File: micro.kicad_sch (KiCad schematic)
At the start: 25 parts, among them SW1 BOOT, SW2 RST, U1 RP2040, U5 W25Q128JVSIQ, Y1 12MHz

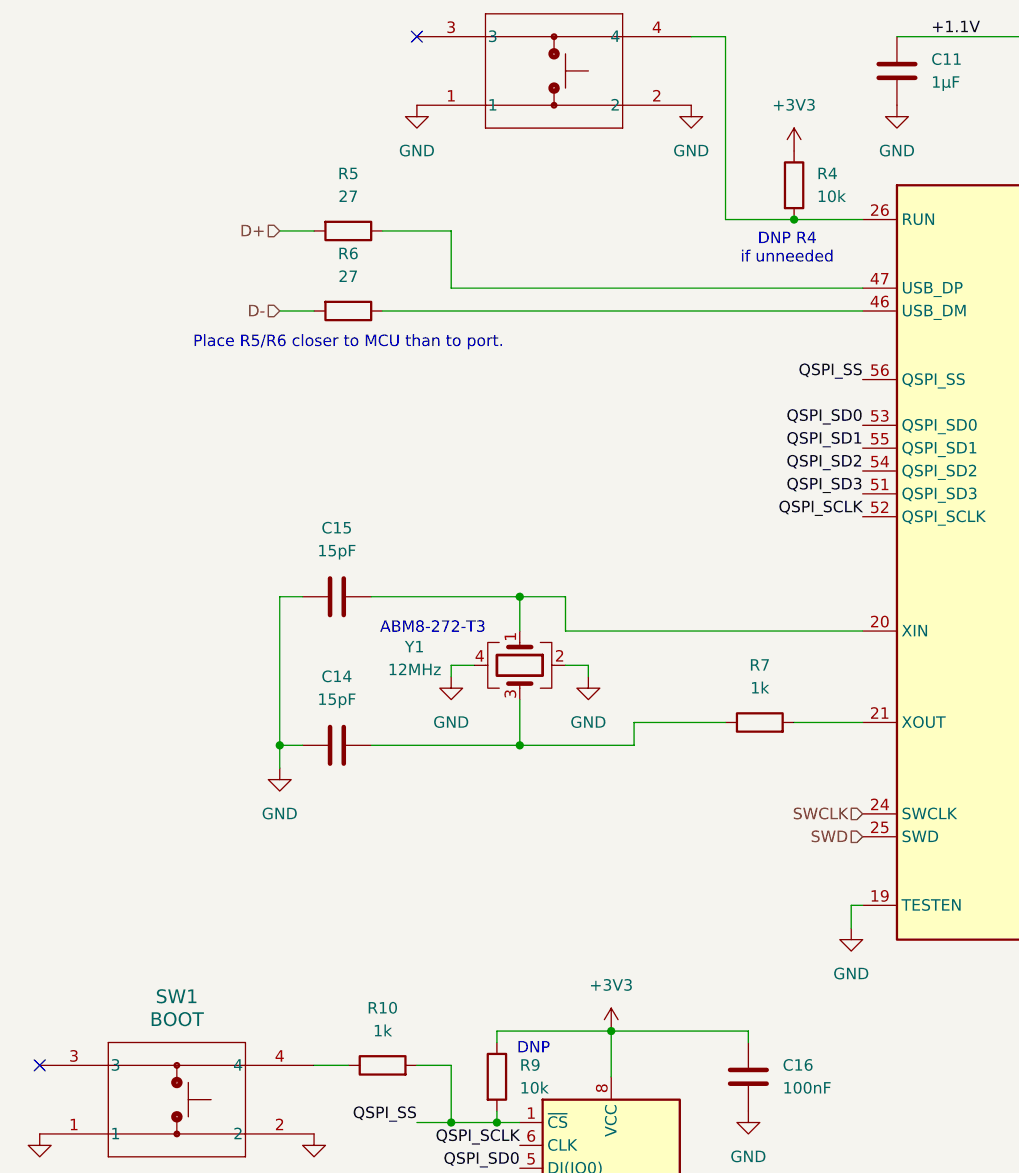
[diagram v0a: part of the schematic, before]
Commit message: WIP: Updated SK6812Mini to SK6812Mini-E and remapped ref des keys between PCB and Schematic.
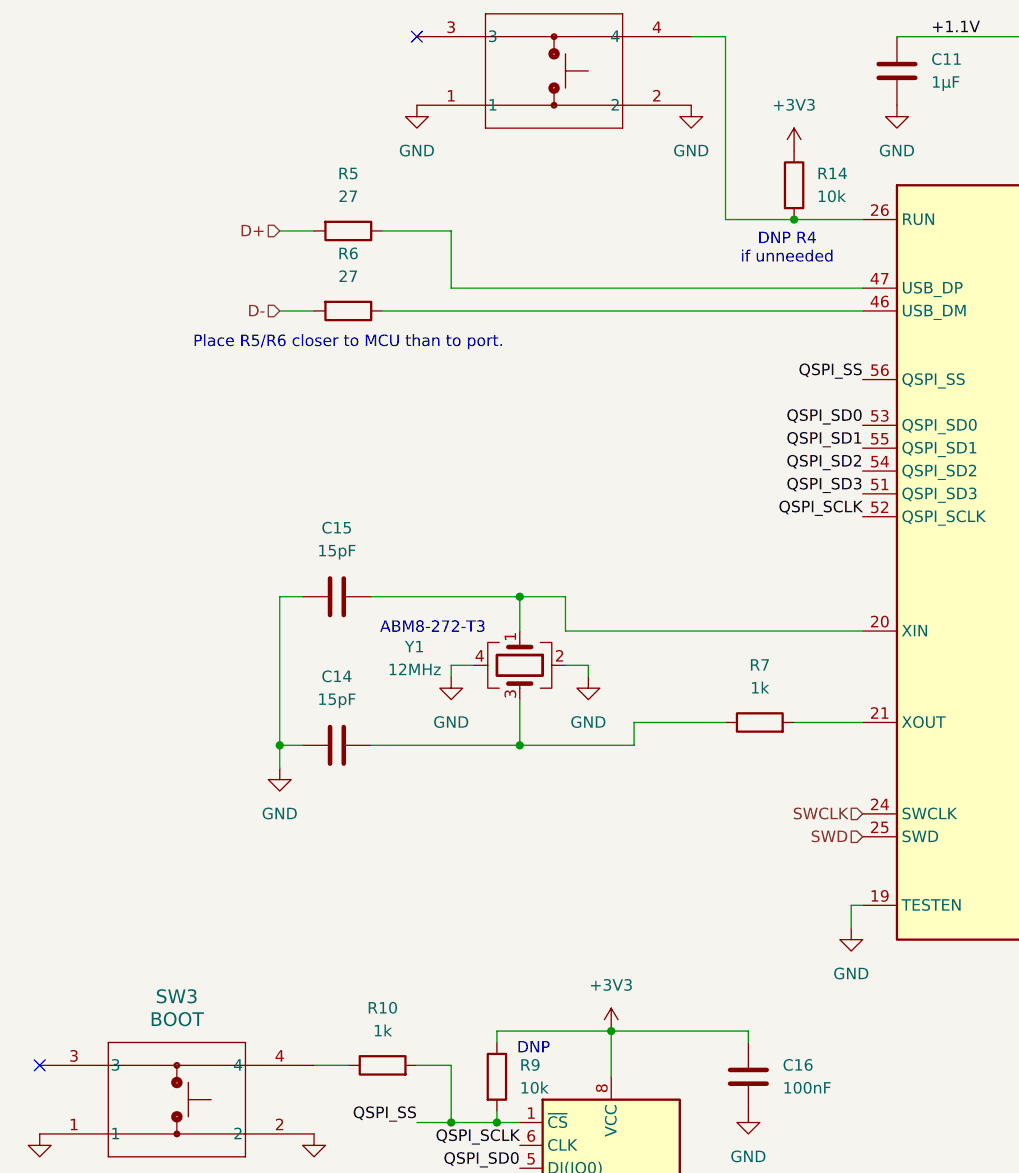
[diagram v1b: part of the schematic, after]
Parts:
- removed R4: 10k, Resistor_SMD:R_0603_1608Metric_Pad0.98x0.95mm_HandSolder, symbol Device:R
- added R14: 10k, Resistor_SMD:R_0603_1608Metric_Pad0.98x0.95mm_HandSolder, symbol Device:R
- renumbered SW1 to SW3
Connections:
- net +3V3: now also R14.1
- net at SW2.4, U1.26 (RUN): now also R14.2
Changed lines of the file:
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@@
 	)
 	(junction
-		(at 119.38 54.61)
-		(diameter 0)
-		(color 0 0 0 0)
-	)
-	(junction
 		(at 160.02 29.21)
 		(diameter 0)
@@
 	)
 	(junction
+		(at 119.38 54.61)
+		(diameter 0)
+		(color 0 0 0 0)
+	)
+	(junction
 		(at 204.47 29.21)
 		(diameter 0)
@@
 	(wire
 		(pts
-			(xy 119.38 54.61) (xy 127 54.61)
+			(xy 111.76 54.61) (xy 119.38 54.61)
 		)
 		(stroke
@@
 	(wire
 		(pts
+			(xy 119.38 54.61) (xy 127 54.61)
+		)
+		(stroke
+			(width 0)
+			(type default)
+		)
+	)
+	(wire
+		(pts
 			(xy 86.36 144.78) (xy 99.06 144.78)
 		)
@@
 	(wire
 		(pts
-			(xy 111.76 54.61) (xy 119.38 54.61)
-		)
-		(stroke
-			(width 0)
-			(type default)
-		)
-	)
-	(wire
-		(pts
 			(xy 83.82 104.14) (xy 81.28 104.14)
 		)
@@
 	)
 	(symbol
+		(lib_id "Device:R")
+		(at 119.38 50.8 0)
+		(unit 1)
+		(exclude_from_sim no)
+		(in_bom yes)
+		(on_board yes)
+		(dnp no)
+		(fields_autoplaced yes)
+		(property "Reference" "R14"
+			(at 121.92 49.5299 0)
+			(effects
+				(font
+					(size 1.27 1.27)
+				)
+				(justify left)
+			)
+		)
+		(property "Value" "10k"
+			(at 121.92 52.0699 0)
+			(effects
+				(font
+					(size 1.27 1.27)
+				)
+				(justify left)
+			)
+		)
+		(property "Footprint" "Resistor_SMD:R_0603_1608Metric_Pad0.98x0.95mm_HandSolder"
+			(at 117.602 50.8 90)
+			(effects
+				(font
+					(size 1.27 1.27)
+				)
+				(hide yes)
+			)
+		)
+		(property "Datasheet" "~"
+			(at 119.38 50.8 0)
+			(effects
+				(font
+					(size 1.27 1.27)
+				)
+				(hide yes)
+			)
+		)
+		(property "Description" "Resistor"
+			(at 119.38 50.8 0)
+			(effects
+				(font
+					(size 1.27 1.27)
+				)
+				(hide yes)
+			)
+		)
+		(pin "1"
+		)
+		(pin "2"
+		)
+		(instances
+			(project "WeddingCenterPieces"
+				(path "/4e0ee48d-0121-4621-a533-4795bdfb88f1/fc5f2ec4-3886-4f1b-8c95-266f3b52f8eb"
+					(reference "R14")
+					(unit 1)
+				)
+			)
+		)
+	)
+	(symbol
 		(lib_id "MCU_RaspberryPi:RP2040")
 		(at 152.4 92.71 0)
@@
 	)
 	(symbol
-		(lib_id "Device:R")
-		(at 119.38 50.8 0)
-		(unit 1)
-		(exclude_from_sim no)
-		(in_bom yes)
-		(on_board yes)
-		(dnp no)
-		(fields_autoplaced yes)
-		(property "Reference" "R4"
-			(at 121.92 49.5299 0)
-			(effects
-				(font
-					(size 1.27 1.27)
-				)
-				(justify left)
-			)
-		)
-		(property "Value" "10k"
-			(at 121.92 52.0699 0)
-			(effects
-				(font
-					(size 1.27 1.27)
-				)
-				(justify left)
-			)
-		)
-		(property "Footprint" "Resistor_SMD:R_0603_1608Metric_Pad0.98x0.95mm_HandSolder"
-			(at 117.602 50.8 90)
-			(effects
-				(font
-					(size 1.27 1.27)
-				)
-				(hide yes)
-			)
-		)
-		(property "Datasheet" "~"
-			(at 119.38 50.8 0)
-			(effects
-				(font
-					(size 1.27 1.27)
-				)
-				(hide yes)
-			)
-		)
-		(property "Description" "Resistor"
-			(at 119.38 50.8 0)
-			(effects
-				(font
-					(size 1.27 1.27)
-				)
-				(hide yes)
-			)
-		)
-		(pin "1"
-		)
-		(pin "2"
-		)
-		(instances
-			(project ""
-				(path "/4e0ee48d-0121-4621-a533-4795bdfb88f1/fc5f2ec4-3886-4f1b-8c95-266f3b52f8eb"
-					(reference "R4")
-					(unit 1)
-				)
-			)
-			(project ""
-				(path "/9203b006-47ac-4f34-8cc4-2b709e3df56f/b2f85b86-5933-4a5f-88c2-315afb4ca3cd"
-					(reference "R4")
-					(unit 1)
-				)
-			)
-		)
-	)
-	(symbol
 		(lib_id "power:GND")
 		(at 66.04 156.21 0)
@@
 		(dnp no)
 		(fields_autoplaced yes)
-		(property "Reference" "SW1"
+		(property "Reference" "SW3"
 			(at 50.8 140.97 0)
 			(effects
@@
 			(project "cheapino"
 				(path "/4e0ee48d-0121-4621-a533-4795bdfb88f1/fc5f2ec4-3886-4f1b-8c95-266f3b52f8eb"
-					(reference "SW1")
+					(reference "SW3")
 					(unit 1)
 				)

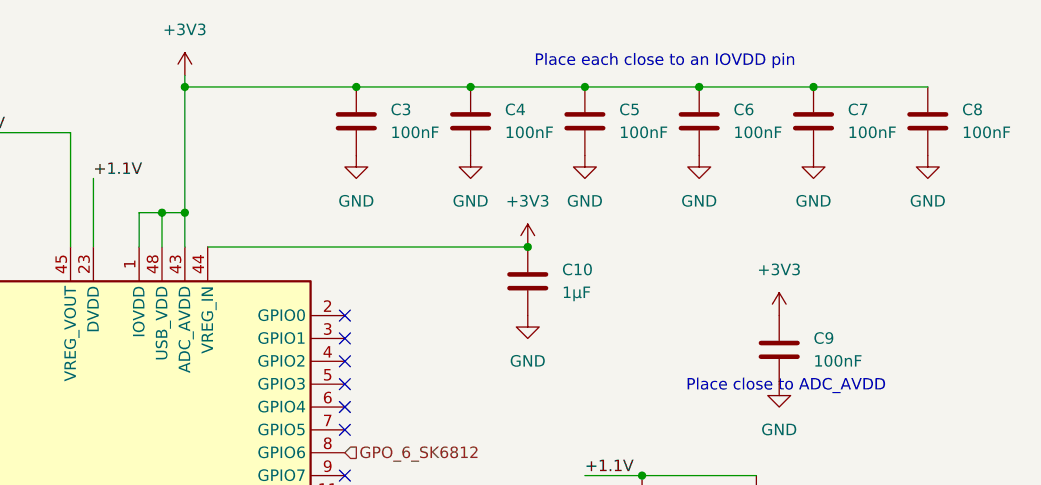
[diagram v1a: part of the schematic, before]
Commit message: Placing nearly all components onto the PCB. Removing the 9Vto5V battery input stage from populating onto the PCB.
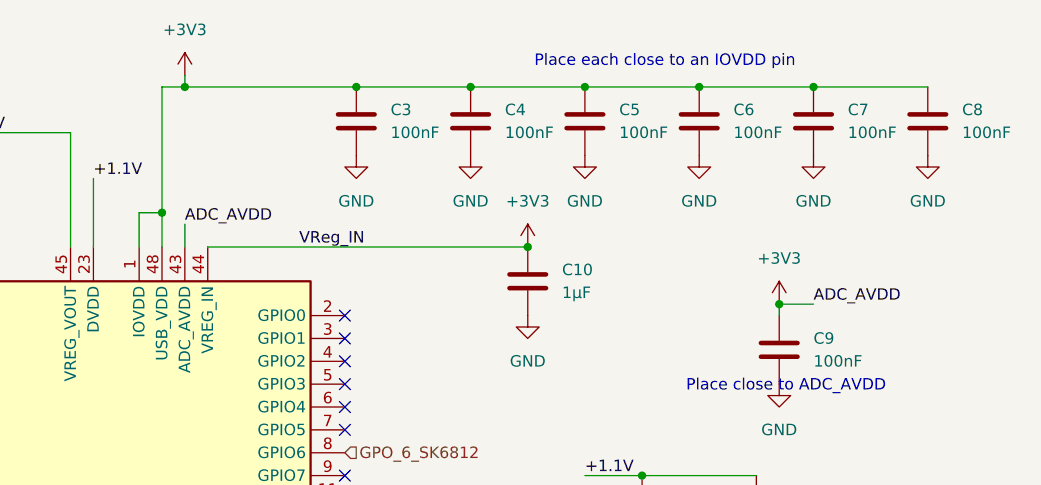
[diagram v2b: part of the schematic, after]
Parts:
- C16: footprint Capacitor_SMD:C_0603_1608Metric_Pad1.08x0.95mm_HandSolder -> Capacitor_SMD:C_0805_2012Metric_Pad1.18x1.45mm_HandSolder
- R10, R14, R5, R6, R9: footprint Resistor_SMD:R_0603_1608Metric_Pad0.98x0.95mm_HandSolder -> Resistor_SMD:R_0805_2012Metric_Pad1.20x1.40mm_HandSolder
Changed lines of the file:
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@@
 	)
 	(junction
-		(at 191.77 29.21)
+		(at 226.06 53.34)
 		(diameter 0)
 		(color 0 0 0 0)
 	)
 	(junction
-		(at 160.02 43.18)
+		(at 191.77 29.21)
 		(diameter 0)
 		(color 0 0 0 0)
@@
 	(wire
 		(pts
+			(xy 157.48 29.21) (xy 160.02 29.21)
+		)
+		(stroke
+			(width 0)
+			(type default)
+		)
+	)
+	(wire
+		(pts
 			(xy 101.6 113.03) (xy 88.9 113.03)
 		)
@@
 	(wire
 		(pts
-			(xy 160.02 46.99) (xy 160.02 43.18)
+			(xy 226.06 53.34) (xy 226.06 54.61)
 		)
 		(stroke
@@
 	(wire
 		(pts
+			(xy 157.48 29.21) (xy 157.48 43.18)
+		)
+		(stroke
+			(width 0)
+			(type default)
+		)
+	)
+	(wire
+		(pts
 			(xy 62.23 115.57) (xy 62.23 113.03)
 		)
@@
 	(wire
 		(pts
-			(xy 160.02 29.21) (xy 160.02 43.18)
+			(xy 229.87 53.34) (xy 226.06 53.34)
 		)
 		(stroke
@@
 	(wire
 		(pts
-			(xy 160.02 43.18) (xy 157.48 43.18)
-		)
-		(stroke
-			(width 0)
-			(type default)
-		)
-	)
-	(wire
-		(pts
 			(xy 157.48 43.18) (xy 157.48 46.99)
 		)
@@
 	(wire
 		(pts
+			(xy 160.02 44.45) (xy 160.02 46.99)
+		)
+		(stroke
+			(width 0)
+			(type default)
+		)
+	)
+	(wire
+		(pts
 			(xy 114.3 144.78) (xy 114.3 146.05)
 		)
@@
 		)
 	)
+	(label "ADC_AVDD"
+		(at 229.87 53.34 0)
+		(fields_autoplaced yes)
+		(effects
+			(font
+				(size 1.27 1.27)
+			)
+			(justify left bottom)
+		)
+	)
 	(label "QSPI_SD1"
 		(at 127 80.01 180)
@@
 		)
 	)
+	(label "ADC_AVDD"
+		(at 160.02 44.45 0)
+		(fields_autoplaced yes)
+		(effects
+			(font
+				(size 1.27 1.27)
+			)
+			(justify left bottom)
+		)
+	)
+	(label "VReg_IN"
+		(at 172.72 46.99 0)
+		(fields_autoplaced yes)
+		(effects
+			(font
+				(size 1.27 1.27)
+			)
+			(justify left bottom)
+		)
+	)
 	(label "QSPI_SD0"
 		(at 127 77.47 180)
@@
 			)
 		)
-		(property "Footprint" "Resistor_SMD:R_0603_1608Metric_Pad0.98x0.95mm_HandSolder"
+		(property "Footprint" "Resistor_SMD:R_0805_2012Metric_Pad1.20x1.40mm_HandSolder"
 			(at 117.602 50.8 90)
 			(effects
@@
 			)
 		)
-		(property "Footprint" "Resistor_SMD:R_0603_1608Metric_Pad0.98x0.95mm_HandSolder"
+		(property "Footprint" "Resistor_SMD:R_0805_2012Metric_Pad1.20x1.40mm_HandSolder"
 			(at 69.85 54.102 90)
 			(effects
@@
 			)
 		)
-		(property "Footprint" "Resistor_SMD:R_0603_1608Metric_Pad0.98x0.95mm_HandSolder"
+		(property "Footprint" "Resistor_SMD:R_0805_2012Metric_Pad1.20x1.40mm_HandSolder"
 			(at 69.85 62.992 90)
 			(effects
@@
 	(symbol
 		(lib_id "power:+3V3")
-		(at 226.06 54.61 0)
+		(at 226.06 53.34 0)
 		(unit 1)
 		(exclude_from_sim no)
@@
 		(fields_autoplaced yes)
 		(property "Reference" "#PWR034"
-			(at 226.06 58.42 0)
+			(at 226.06 57.15 0)
 			(effects
 				(font
@@
 		)
 		(property "Value" "+3V3"
-			(at 226.06 49.53 0)
+			(at 226.06 48.26 0)
 			(effects
 				(font
@@
 		)
 		(property "Footprint" ""
-			(at 226.06 54.61 0)
+			(at 226.06 53.34 0)
 			(effects
 				(font
@@
 		)
 		(property "Datasheet" ""
-			(at 226.06 54.61 0)
+			(at 226.06 53.34 0)
 			(effects
 				(font
@@
 		)
 		(property "Description" "Power symbol creates a global label with name \"+3V3\""
-			(at 226.06 54.61 0)
+			(at 226.06 53.34 0)
 			(effects
 				(font
@@
 			)
 		)
-		(property "Footprint" "Capacitor_SMD:C_0603_1608Metric_Pad1.08x0.95mm_HandSolder"
+		(property "Footprint" "Capacitor_SMD:C_0805_2012Metric_Pad1.18x1.45mm_HandSolder"
 			(at 115.2652 153.67 0)
 			(effects
@@
 			)
 		)
-		(property "Footprint" "Resistor_SMD:R_0603_1608Metric_Pad0.98x0.95mm_HandSolder"
+		(property "Footprint" "Resistor_SMD:R_0805_2012Metric_Pad1.20x1.40mm_HandSolder"
 			(at 73.66 150.368 90)
 			(effects
@@
 			)
 		)
-		(property "Footprint" "Resistor_SMD:R_0603_1608Metric_Pad0.98x0.95mm_HandSolder"
+		(property "Footprint" "Resistor_SMD:R_0805_2012Metric_Pad1.20x1.40mm_HandSolder"
 			(at 84.582 149.86 90)
 			(effects

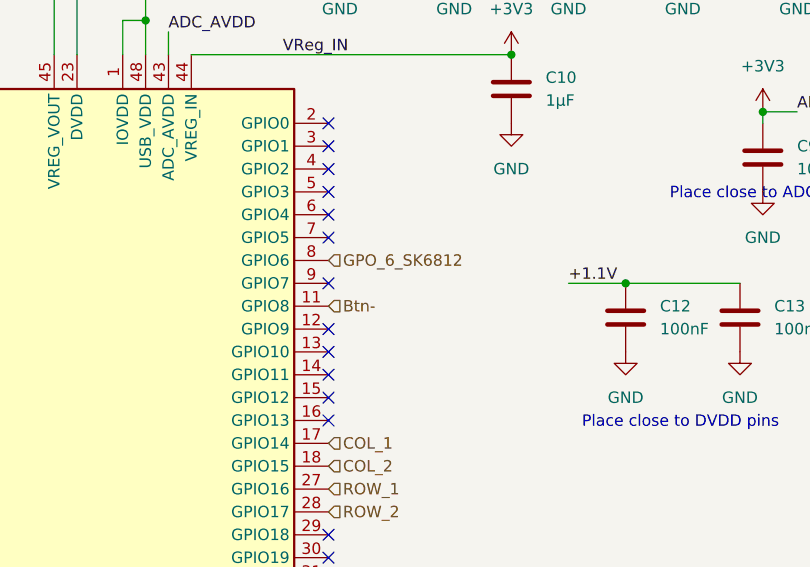
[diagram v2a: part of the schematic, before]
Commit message: Adding additional LEDs and driver to test per-key LEDs, updating net classes and design constraints, and starting to route tracks.
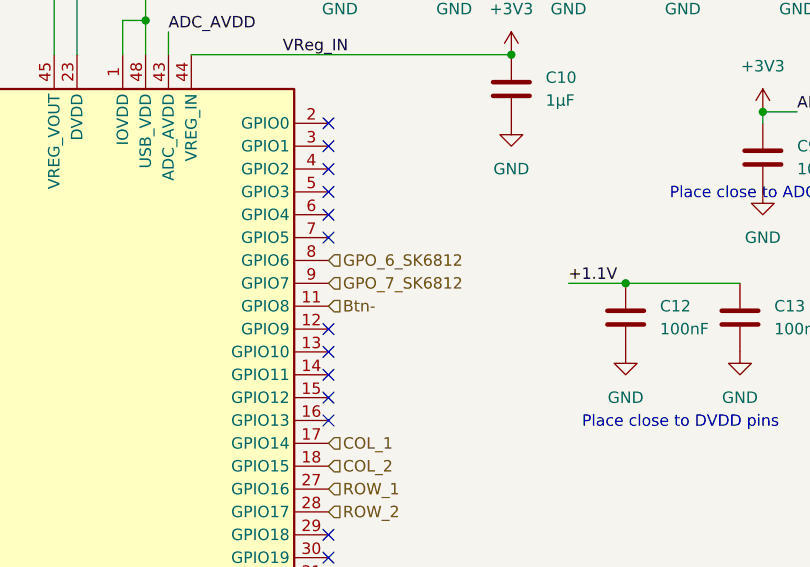
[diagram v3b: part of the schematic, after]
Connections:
- net GPO_7_SK6812: now reaches U1.9 (GPIO7)
- no-connect marks 25 -> 24
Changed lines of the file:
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@@
 		(at 177.8 54.61)
-	)
-	(no_connect
-		(at 177.8 72.39)
 	)
 	(wire
@@
 		)
 	)
+	(hierarchical_label "GPO_7_SK6812"
+		(shape input)
+		(at 177.8 72.39 0)
+		(fields_autoplaced yes)
+		(effects
+			(font
+				(size 1.27 1.27)
+			)
+			(justify left)
+		)
+	)
 	(hierarchical_label "D-"
 		(shape input)
@@
 		)
 	)
+	(netclass_flag ""
+		(length 2.54)
+		(shape dot)
+		(at 101.6 62.23 0)
+		(fields_autoplaced yes)
+		(effects
+			(font
+				(size 1.27 1.27)
+			)
+			(justify left bottom)
+		)
+		(property "Netclass" "USB_Data"
+			(at 102.2985 59.69 0)
+			(effects
+				(font
+					(size 1.27 1.27)
+					(italic yes)
+				)
+				(justify left)
+			)
+		)
+	)
+	(netclass_flag ""
+		(length 2.54)
+		(shape dot)
+		(at 101.6 64.77 180)
+		(fields_autoplaced yes)
+		(effects
+			(font
+				(size 1.27 1.27)
+			)
+			(justify right bottom)
+		)
+		(property "Netclass" "USB_Data"
+			(at 102.2985 67.31 0)
+			(effects
+				(font
+					(size 1.27 1.27)
+					(italic yes)
+				)
+				(justify left)
+			)
+		)
+	)

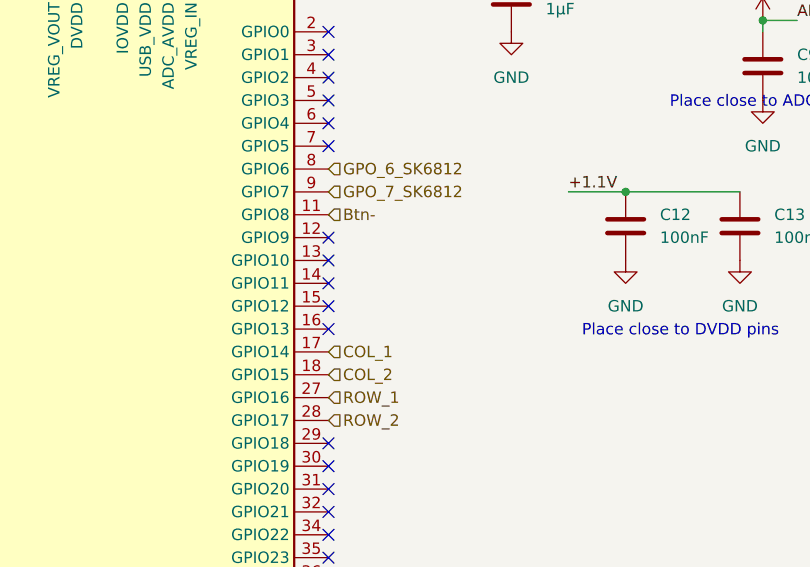
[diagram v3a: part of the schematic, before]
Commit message: Shrinking board to only have 2 key switches and a few other unnecessary components. Finished with routing the rest of the board.
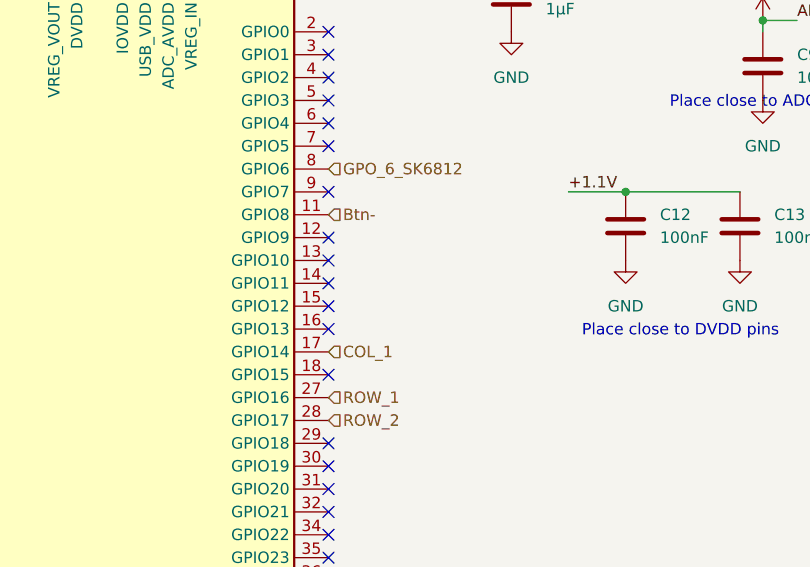
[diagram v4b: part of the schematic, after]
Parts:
- R5, R6: footprint Resistor_SMD:R_0805_2012Metric_Pad1.20x1.40mm_HandSolder -> Resistor_SMD:R_0603_1608Metric_Pad0.98x0.95mm_HandSolder
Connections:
- net COL_2: no longer names the net of U1.18 (GPIO15)
- net GPO_7_SK6812: no longer names the net of U1.9 (GPIO7)
- no-connect marks 24 -> 26
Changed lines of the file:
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@@
+	)
+	(no_connect
+		(at 177.8 92.71)
 	)
 	(no_connect
@@
 	(no_connect
 		(at 177.8 80.01)
+	)
+	(no_connect
+		(at 177.8 72.39)
 	)
 	(no_connect
@@
 		)
 	)
-	(hierarchical_label "GPO_7_SK6812"
-		(shape input)
-		(at 177.8 72.39 0)
-		(fields_autoplaced yes)
-		(effects
-			(font
-				(size 1.27 1.27)
-			)
-			(justify left)
-		)
-	)
 	(hierarchical_label "D-"
 		(shape input)
@@
 		(shape input)
 		(at 177.8 74.93 0)
-		(fields_autoplaced yes)
-		(effects
-			(font
-				(size 1.27 1.27)
-			)
-			(justify left)
-		)
-	)
-	(hierarchical_label "COL_2"
-		(shape input)
-		(at 177.8 92.71 0)
 		(fields_autoplaced yes)
 		(effects
@@
 			)
 		)
-		(property "Footprint" "Resistor_SMD:R_0805_2012Metric_Pad1.20x1.40mm_HandSolder"
+		(property "Footprint" "Resistor_SMD:R_0603_1608Metric_Pad0.98x0.95mm_HandSolder"
 			(at 69.85 54.102 90)
 			(effects
@@
 			)
 		)
-		(property "Footprint" "Resistor_SMD:R_0805_2012Metric_Pad1.20x1.40mm_HandSolder"
+		(property "Footprint" "Resistor_SMD:R_0603_1608Metric_Pad0.98x0.95mm_HandSolder"
 			(at 69.85 62.992 90)
 			(effects
